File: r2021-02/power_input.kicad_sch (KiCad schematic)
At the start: 23 parts

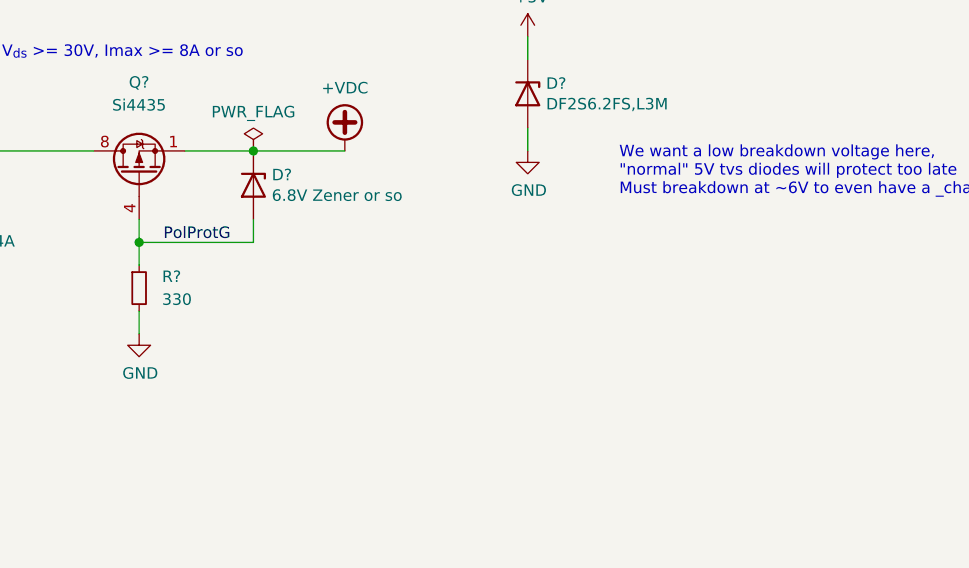
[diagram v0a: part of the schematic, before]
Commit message: hw: r2: clarify parts and values for polarity protection
falstad simulation:

$ 1 0.000005 10.20027730826997 50 5 50 5e-11
34 zener-5.6 1 1.7143528192810002e-7 0 2.0000000000000084 10 1
z 416 208 416 128 2 zener-5.6
f 288 208 288 128 33 1.5 0.02
r 288 256 288 304 0 10000
r 528 144 528 304 0 10
w 304 128 416 128 0
w 288 208 288 224 0
w 416 128 528 144 0
w 416 208 288 208 0
w 528 304 288 304 0
v 64 224 64 160 0 0 40 30 0 0 0.5
w 160 112 272 128 0
w 128 304 288 304 0
v 112 160 112 224 0 0 40 12 0 0 0.5
w 64 224 128 304 0
w 112 224 128 304 0
S 160 112 112 112 0 1 false 0 2
w 112 128 112 160 0
w 112 96 64 160 0
368 272 128 272 64 0 0
368 416 128 368 64 0 0
p 288 208 416 128 1 0 0
370 288 224 288 256 1 0 0
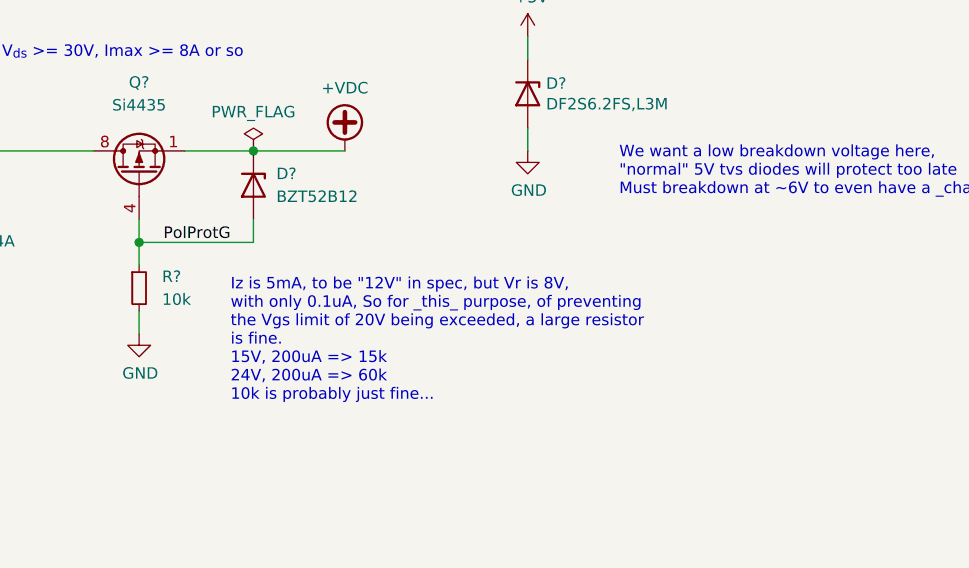
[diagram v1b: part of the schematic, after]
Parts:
- removed D?: 6.8V Zener or so, Diode_SMD:D_SOD-123F, symbol Device:D_Zener
- added D?: BZT52B12, Diode_SMD:D_SOD-123, symbol Diode:BZT52Bxx
- R?: value 330 -> 10k
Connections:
- net +VDC: now also D?.1 (K)
- net PolProtG: now also D?.2 (A)
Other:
- note added: "Iz is 5mA, to be "12V" in spec, but Vr is 8V, with only 0.1uA, So for _this_ purpose, of preventing the Vgs limit of 20V being exceeded, a large resistor is fine. 15V, 200uA => 15k 24V, 200uA => 60k 10k is probably just fine..."
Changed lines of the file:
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@@
+    (effects (font (size 1.27 1.27)) (justify left bottom))
+  )
+  (text "Iz is 5mA, to be \"12V\" in spec, but Vr is 8V,\nwith only 0.1uA, So for _this_ purpose, of preventing\nthe Vgs limit of 20V being exceeded, a large resistor\nis fine.\n15V, 200uA => 15k\n24V, 200uA => 60k\n10k is probably just fine..."
+    (at 109.22 68.58 0)
     (effects (font (size 1.27 1.27)) (justify left bottom))
   )
@@
     (pin "1")
   )
-  (symbol (lib_id "Device:D_Zener") (at 111.76 44.45 270) (unit 1)
-    (in_bom yes) (on_board yes)
-    (property "Reference" "D?" (id 0) (at 113.792 43.307 90)
-      (effects (font (size 1.27 1.27)) (justify left))
-    )
-    (property "Value" "6.8V Zener or so" (id 1) (at 113.792 45.593 90)
-      (effects (font (size 1.27 1.27)) (justify left))
-    )
-    (property "Footprint" "Diode_SMD:D_SOD-123F" (id 2) (at 111.76 44.45 0)
-      (effects (font (size 1.27 1.27)) hide)
-    )
-    (property "Datasheet" "~" (id 3) (at 111.76 44.45 0)
-      (effects (font (size 1.27 1.27)) hide)
-    )
-    (pin "1")
-    (pin "2")
-  )
   (symbol (lib_id "power:GND") (at 60.96 172.72 0) (unit 1)
     (in_bom yes) (on_board yes)
@@
     (pin "2")
   )
+  (symbol (lib_id "Diode:BZT52Bxx") (at 111.76 44.45 270) (unit 1)
+    (in_bom yes) (on_board yes) (fields_autoplaced)
+    (property "Reference" "D?" (id 0) (at 114.3 43.1799 90)
+      (effects (font (size 1.27 1.27)) (justify left))
+    )
+    (property "Value" "BZT52B12" (id 1) (at 114.3 45.7199 90)
+      (effects (font (size 1.27 1.27)) (justify left))
+    )
+    (property "Footprint" "Diode_SMD:D_SOD-123" (id 2) (at 107.315 44.45 0)
+      (effects (font (size 1.27 1.27)) hide)
+    )
+    (property "Datasheet" "https://diotec.com/tl_files/diotec/files/pdf/datasheets/bzt52b2v4.pdf" (id 3) (at 111.76 44.45 0)
+      (effects (font (size 1.27 1.27)) hide)
+    )
+    (property "MPN" "BZT52-C12" (id 4) (at 111.76 44.45 90)
+      (effects (font (size 1.27 1.27)) hide)
+    )
+    (pin "1")
+    (pin "2")
+  )
   (symbol (lib_id "Device:C_Small") (at 93.98 163.83 180) (unit 1)
     (in_bom yes) (on_board yes)
@@
       (effects (font (size 1.27 1.27)) (justify left))
     )
-    (property "Value" "330" (id 1) (at 101.6 57.15 0)
+    (property "Value" "10k" (id 1) (at 101.6 57.15 0)
       (effects (font (size 1.27 1.27)) (justify left))
     )

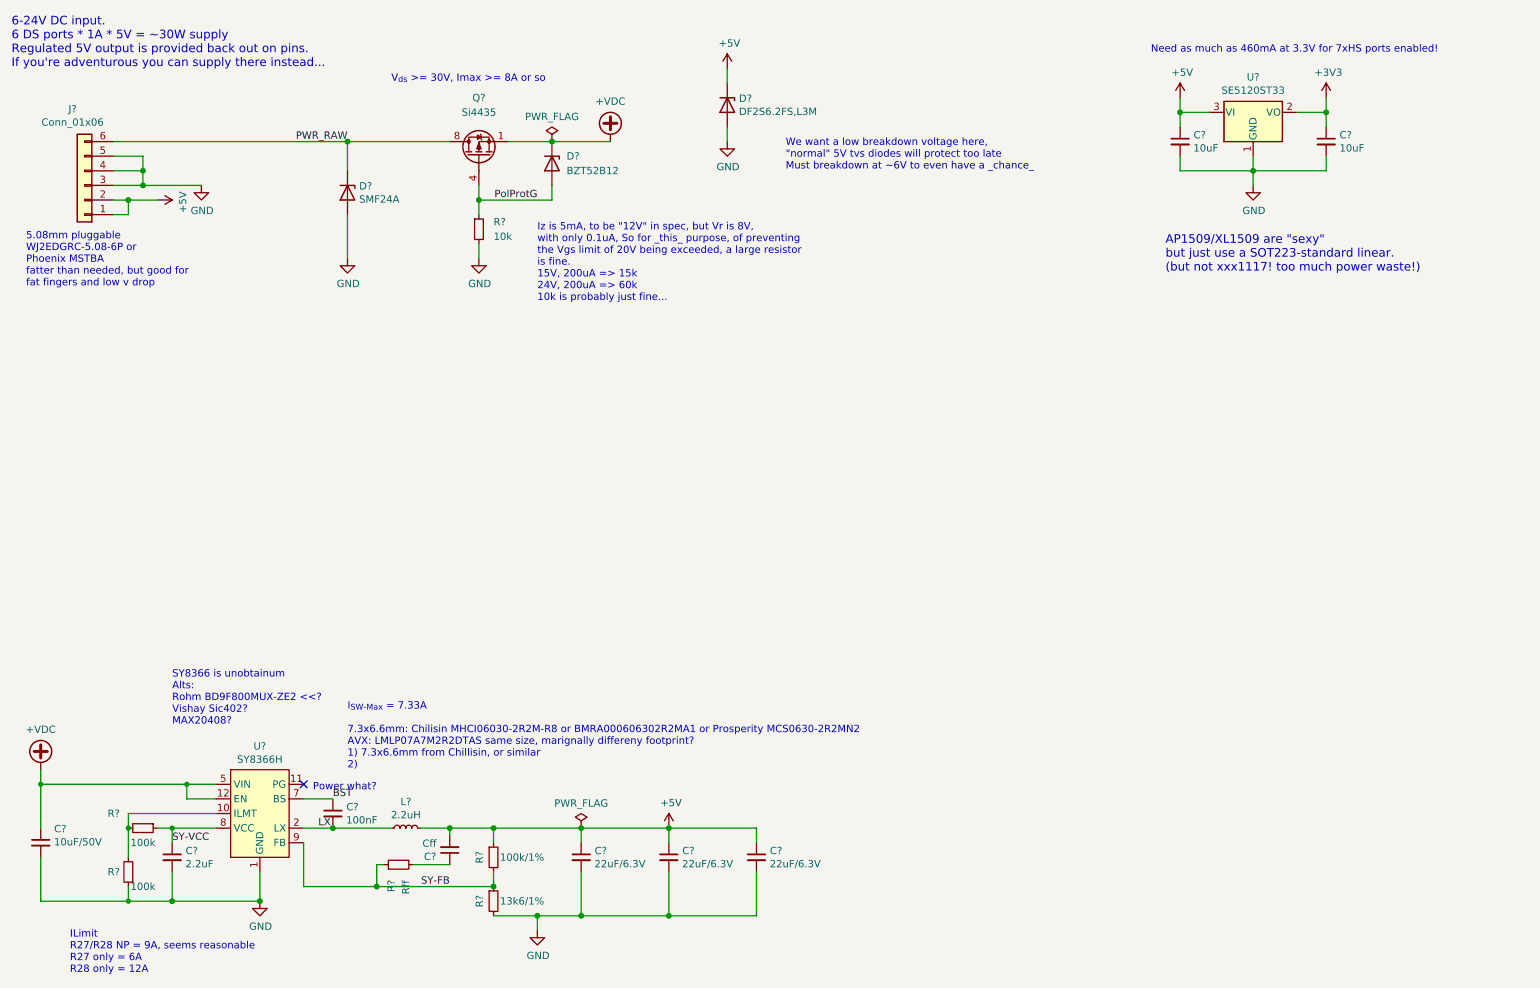
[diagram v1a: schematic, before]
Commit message: hw: r2: use SiC437 for power supply
Overhaul heavily.  Schematic largely complete for changes, but needs
review, PCB barely started.
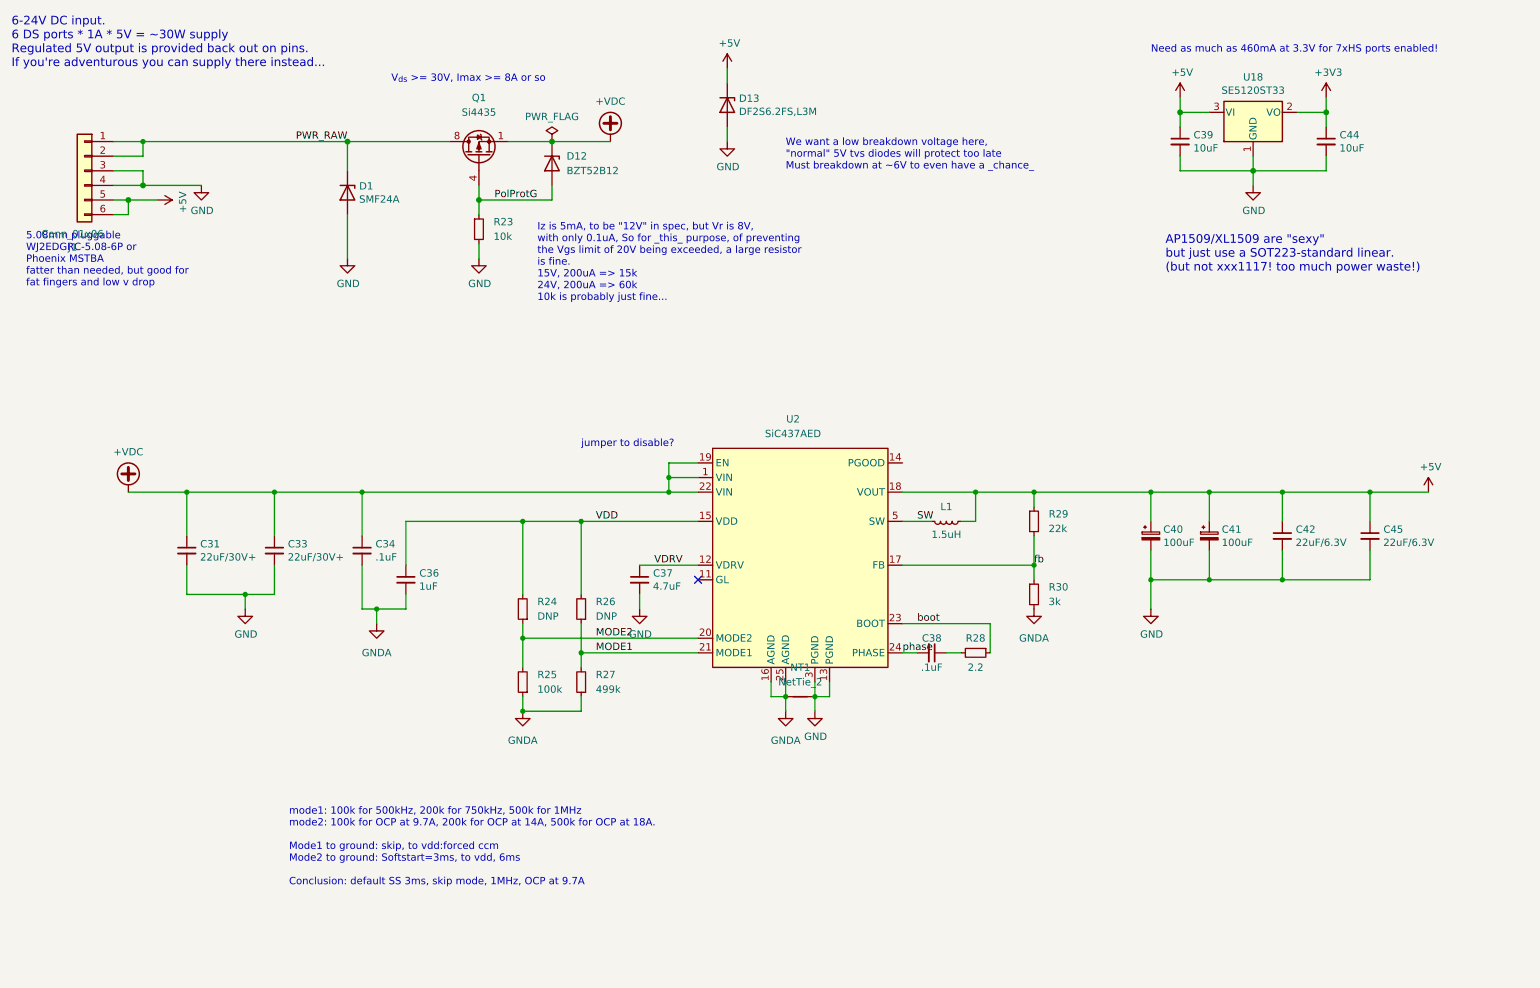
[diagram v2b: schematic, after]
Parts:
- removed C? (x3): 22uF/6.3V, Capacitor_SMD:C_0805_2012Metric, symbol Device:C_Small
- removed C?: Cff, Capacitor_SMD:C_0603_1608Metric, symbol Device:C_Small
- removed C?: 100nF, Capacitor_SMD:C_0603_1608Metric, symbol Device:C_Small
- removed C?: 2.2uF, Capacitor_SMD:C_0603_1608Metric, symbol Device:C_Small
- removed C?: 10uF/50V, Capacitor_SMD:C_0805_2012Metric, symbol Device:C_Small
- removed R?: 13k6/1%, Resistor_SMD:R_0603_1608Metric, symbol Device:R_Small
- removed R?: Rff, Resistor_SMD:R_0603_1608Metric, symbol Device:R_Small
- removed R? (x2): 100k, Resistor_SMD:R_0603_1608Metric, symbol Device:R_Small
- removed R?: 100k/1%, Resistor_SMD:R_0603_1608Metric, symbol Device:R_Small
- removed U?: SY8366H, et-parts:SY8366H, symbol etactica-parts:SY8366H
- added C31, C33: 22uF/30V+, Capacitor_SMD:C_0805_2012Metric, symbol Device:C_Small
- added C34, C38: .1uF, Capacitor_SMD:C_0603_1608Metric, symbol Device:C_Small
- added C36: 1uF, Capacitor_SMD:C_0603_1608Metric, symbol Device:C_Small
- added C37: 4.7uF, Capacitor_SMD:C_0603_1608Metric, symbol Device:C_Small
- added C40, C41: 100uF, Capacitor_SMD:CP_Elec_5x5.4, symbol Device:C_Polarized_Small
- added C42, C45: 22uF/6.3V, Capacitor_SMD:C_0805_2012Metric, symbol Device:C_Small
- added NT1: NetTie_2, symbol Device:NetTie_2
- added R24, R26: DNP, Resistor_SMD:R_0603_1608Metric, symbol Device:R_Small
- added R25: 100k, Resistor_SMD:R_0603_1608Metric, symbol Device:R_Small
- added R27: 499k, Resistor_SMD:R_0603_1608Metric, symbol Device:R_Small
- added R28: 2.2, Resistor_SMD:R_0603_1608Metric, symbol Device:R_Small
- added R29: 22k, Resistor_SMD:R_0603_1608Metric, symbol Device:R_Small
- added R30: 3k, Resistor_SMD:R_0603_1608Metric, symbol Device:R_Small
- added U2: SiC437AED, Package_DFN_QFN:Vishay_MLP-44L_4x4, symbol Regulator_Switching:SiC437AED
- L1: renamed from L?; value 2.2uH -> 1.5uH; footprint Inductor_SMD:L_CHILISIN_BMRx00060630 -> Inductor_SMD:L_AVX_LMLP07A7; MPN MHCI06030-2R2M-R8 -> LMLP07A7M1R5DTAS
- gave numbers to parts that had none: 9
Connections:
- net LX is gone; now on net +5V: L1.1
- net +5V: now also J1.5 (Pin_5), J1.6 (Pin_6), C40.1, C41.1, C42.1, C45.1, R29.1, U2.18 (VOUT); no longer J1.1 (Pin_1), J1.2 (Pin_2), L1.2
- net +VDC: now also C31.1, C33.1, C34.1, U2.1 (VIN), U2.19 (EN), U2.22 (VIN)
- net GND: now also C31.2, C33.2, C37.2, C40.2, C41.2, C42.2, C45.2, NT1.2, U2.13 (PGND), U2.3 (PGND); no longer J1.5 (Pin_5)
- net PWR_RAW: now also J1.1 (Pin_1), J1.2 (Pin_2); no longer J1.6 (Pin_6)
- new net: C38.1, R28.2
- new net GNDA: C34.2, C36.2, NT1.1, R25.1, R27.1, R30.2, U2.16 (AGND), U2.25 (AGND)
- new net MODE1: R26.1, R27.2, U2.21 (MODE1)
- new net MODE2: R24.1, R25.2, U2.20 (MODE2)
- new net SW: L1.2, U2.5 (SW)
- new net VDD: C36.1, R24.2, R26.2, U2.15 (VDD)
- new net VDRV: C37.1, U2.12 (VDRV)
- new net boot: R28.1, U2.23 (BOOT)
- new net fb: R29.2, R30.1, U2.17 (FB)
- new net phase: C38.2, U2.24 (PHASE)
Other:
- note added: "jumper to disable?"
- note added: "mode1: 100k for 500kHz, 200k for 750kHz, 500k for 1MHz mode2: 100k for OCP at 9.7A, 200k for OCP at 14A, 500k for OCP at 18A. Mode1 to ground: skip, to vdd:forced ccm Mode2 to ground: Softstart=3ms, to vdd, 6ms Conclusion: default SS 3ms, skip mode, 1MHz, OCP at 9.7A"
- note removed: "ILimit R27/R28 NP = 9A, seems reasonable R27 only = 6A R28 only = 12A"
- note removed: "I_{SW-Max} = 7.33A 7.3x6.6mm: Chilisin MHCI06030-2R2M-R8 or BMRA000606302R2MA1 or Prosperity MCS0630-2R2MN2 AVX: LMLP07A7M2R2DTAS same size, marignally differeny footprint? 1) 7.3x6.6mm from Chillisin, or similar 2)"
- note removed: "Power what?"
- note removed: "SY8366 is unobtainum Alts: Rohm BD9F800MUX-ZE2 <<? Vishay Sic402? MAX20408?"
- moved on the sheet: J1, L1

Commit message: restore to kicad 6.0 compatibility
updated to my footprintbranch, 6.0 and all that
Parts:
- NT1: footprint (none) -> NetTie:NetTie-2_SMD_Pad0.5mm

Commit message: hubbish-r2: shrink to 100x80
re-connect all the parts, and continue to shirk responsibilities to
route the power supply again.
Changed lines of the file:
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@@
   )
   (text "5.08mm pluggable\nWJ2EDGRC-5.08-6P or\nPhoenix MSTBA\nfatter than needed, but good for\nfat fingers and low v drop\n"
-    (at 20.32 66.04 0)
+    (at 21.59 71.12 0)
     (effects (font (size 1.27 1.27)) (justify left bottom))
   )

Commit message: r2: start really doing some power routing...
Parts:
- removed NT1: NetTie_2, NetTie:NetTie-2_SMD_Pad0.5mm, symbol Device:NetTie_2
- U2: value SiC437AED -> (none); footprint Package_DFN_QFN:Vishay_MLP-44L_4x4 -> (none)
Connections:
- net GNDA is gone; now on net GND: C34.2, C36.2, R25.1, R27.1, R30.2, U2.16 (AGND), U2.25 (AGND)
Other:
- note added: "Yes, no net tie. See the datasheet, they want a single pour connecting them, even though they talk about splitting the ground plane on inner/lower layers for isolation..."
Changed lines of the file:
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@@
+    (stroke (width 0) (type default) (color 0 0 0 0))
+  )
+  (wire (pts (xy 152.4 137.16) (xy 157.48 137.16))
     (stroke (width 0) (type default) (color 0 0 0 0))
   )
@@
   )
   (text "V_{ds} >= 30V, Imax >= 8A or so" (at 83.82 30.48 0)
+    (effects (font (size 1.27 1.27)) (justify left bottom))
+  )
+  (text "Yes, no net tie.\nSee the datasheet, they want a single pour connecting\nthem, even though they talk about splitting the ground\nplane on inner/lower layers for isolation..."
+    (at 143.51 153.67 0)
     (effects (font (size 1.27 1.27)) (justify left bottom))
   )
@@
     (in_bom yes) (on_board yes) (fields_autoplaced)
     (property "Reference" "U2" (id 0) (at 153.67 88.9 0))
-    (property "Value" "SiC437AED" (id 1) (at 153.67 91.44 0))
-    (property "Footprint" "Package_DFN_QFN:Vishay_MLP-44L_4x4" (id 2) (at 154.94 101.6 0)
+    (property "Value" "" (id 1) (at 153.67 91.44 0))
+    (property "Footprint" "" (id 2) (at 154.94 101.6 0)
       (effects (font (size 1.27 1.27)) hide)
     )
@@
       (effects (font (size 1.27 1.27)) hide)
     )
-    (pin "1")
-    (pin "2")
-  )
-  (symbol (lib_id "Device:NetTie_2") (at 154.94 137.16 0) (unit 1)
-    (in_bom yes) (on_board yes) (fields_autoplaced)
-    (property "Reference" "NT1" (id 0) (at 154.94 132.08 0))
-    (property "Value" "NetTie_2" (id 1) (at 154.94 134.62 0))
-    (property "Footprint" "NetTie:NetTie-2_SMD_Pad0.5mm" (id 2) (at 154.94 137.16 0)
-      (effects (font (size 1.27 1.27)) hide)
-    )
-    (property "Datasheet" "~" (id 3) (at 154.94 137.16 0)
-      (effects (font (size 1.27 1.27)) hide)
-    )

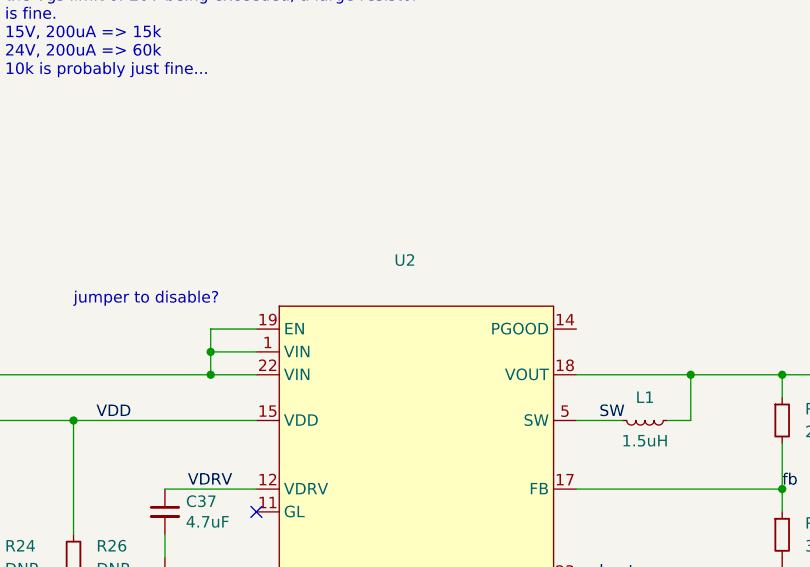
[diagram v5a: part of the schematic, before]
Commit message: "finished" rev2?
ok, should we go and order this damn thing?  try it one more time?

M2.5, should i use m3?
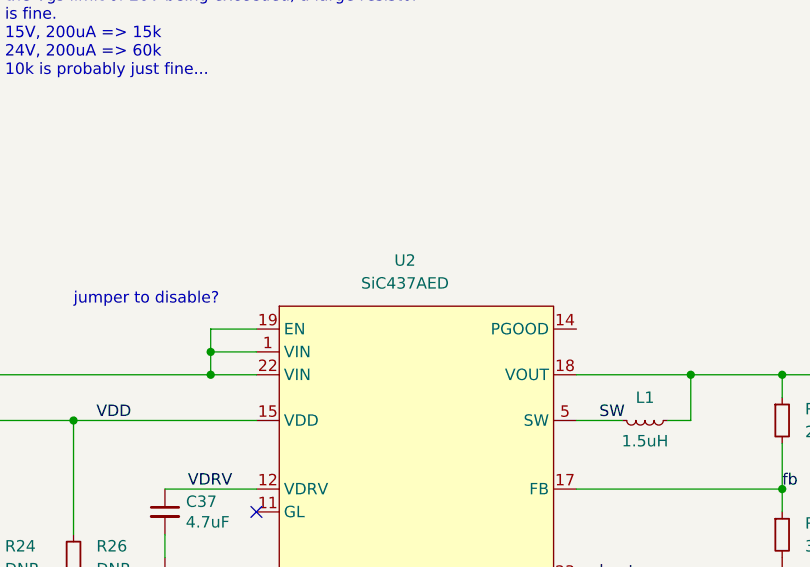
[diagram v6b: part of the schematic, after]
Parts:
- U2: value (none) -> SiC437AED; footprint (none) -> Package_DFN_QFN:Vishay_MLP-44L_4x4
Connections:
- net at U2.11 (GL): now also U2.10 (GL), U2.28 (GL)
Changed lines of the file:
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@@
     (in_bom yes) (on_board yes) (fields_autoplaced)
     (property "Reference" "U2" (id 0) (at 153.67 88.9 0))
-    (property "Value" "" (id 1) (at 153.67 91.44 0))
-    (property "Footprint" "" (id 2) (at 154.94 101.6 0)
+    (property "Value" "SiC437AED" (id 1) (at 153.67 91.44 0))
+    (property "Footprint" "Package_DFN_QFN:Vishay_MLP-44L_4x4" (id 2) (at 154.94 101.6 0)
       (effects (font (size 1.27 1.27)) hide)
     )
@@
       (effects (font (size 1.27 1.27)) hide)
     )
+    (pin "10")
     (pin "11")
     (pin "12")
     (pin "13")
     (pin "19")
+    (pin "28")
     (pin "5")
     (pin "1")

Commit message: overhaul, push silk, complete "again"
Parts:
- renumbered C31 to C34, C33 to C35, C34 to C36, C36 to C37, C37 to C38, C38 to C39, C39 to C41, C41 to C42, C42 to C43, D1 to D11, J1 to J8, U2 to U18, U18 to U19
